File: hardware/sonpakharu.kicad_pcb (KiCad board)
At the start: 2 copper layers, 51.3 x 71.1 mm, 70 parts, among them IC1 ESP32-S3-WROOM-1U-N4, J1 ADC4, J10 EXT2, J11 EXT3, J12 BATT, J13 EXT7, J14 PWR, J15 EXT8, J16 485, J17 FTDI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

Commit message: Fix: final fixes
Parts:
- moved sp 1.67 mm to (126.9, 64.9)
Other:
- board text added: "Sonpakhru"
- board text added: "sonpakhru.com"
- board text removed: "Sonpakharu"

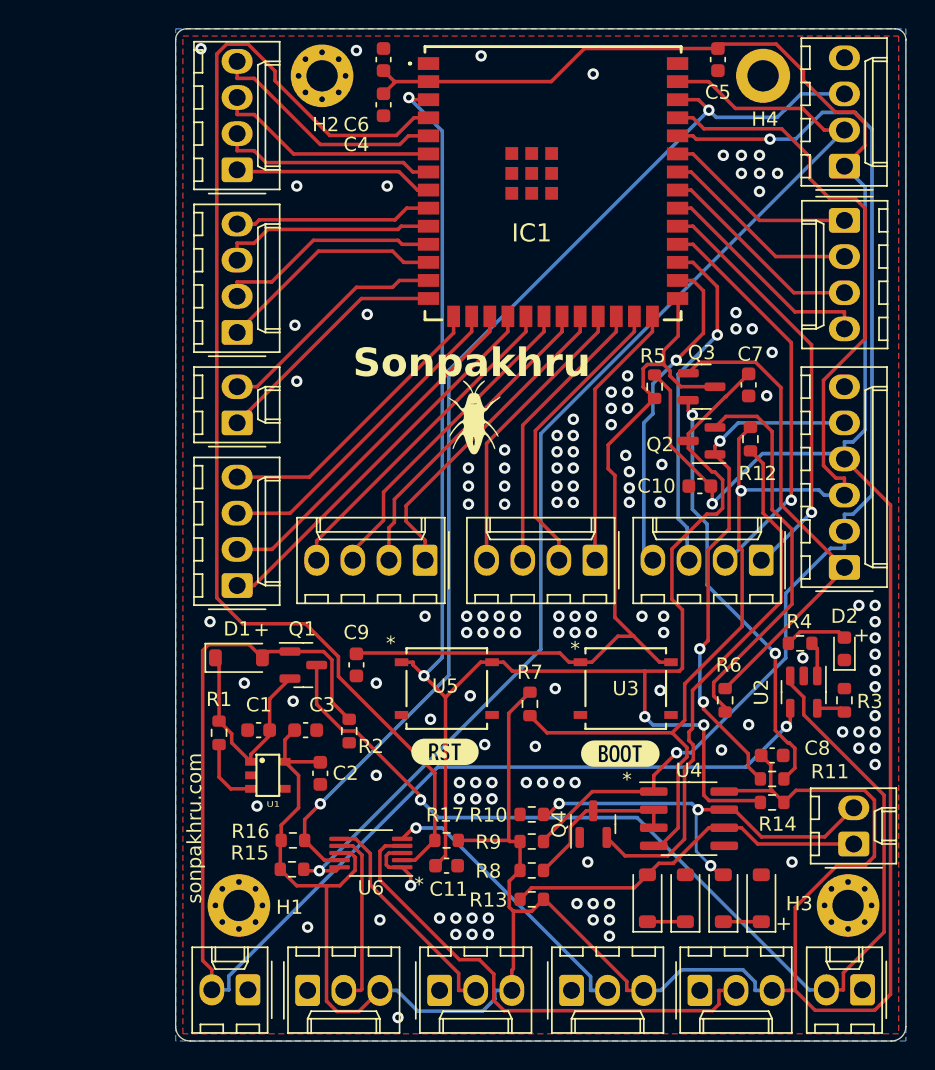
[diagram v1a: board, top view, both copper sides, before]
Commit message: rectified sch
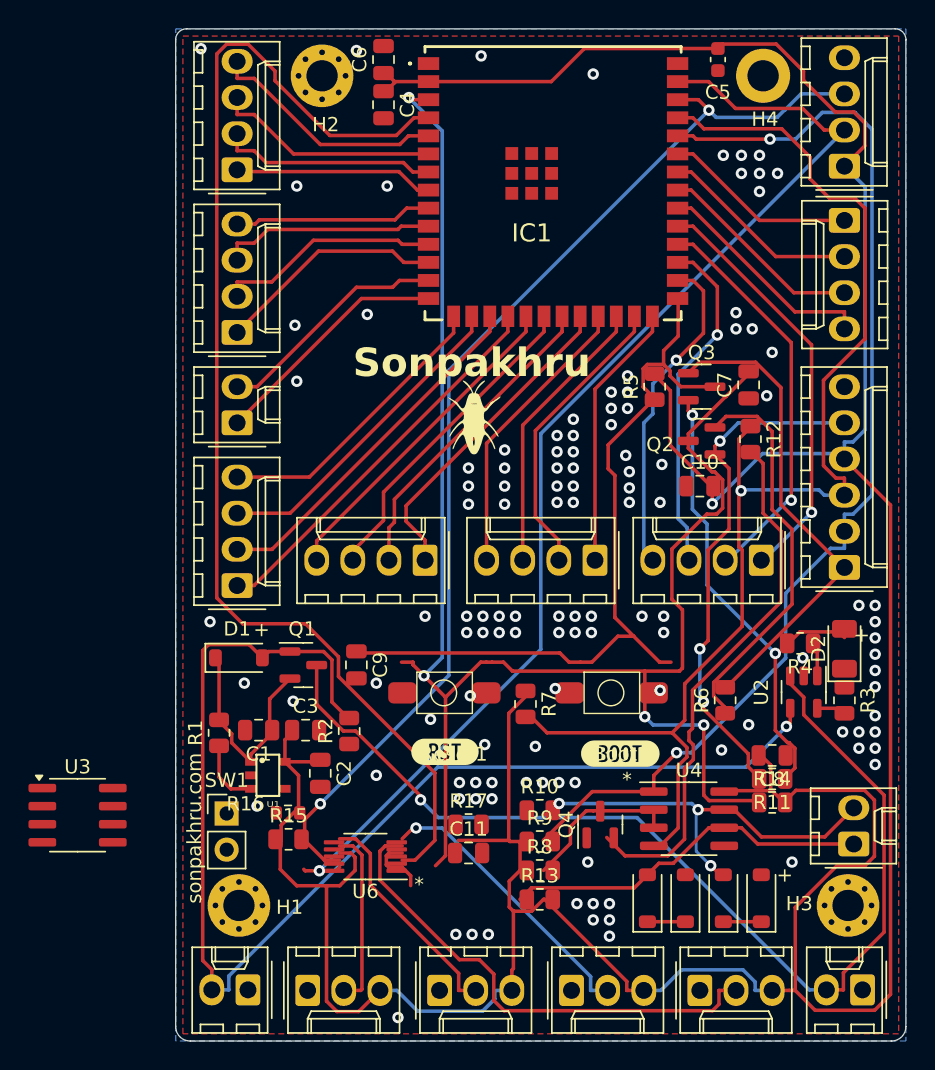
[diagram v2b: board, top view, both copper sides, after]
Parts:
- removed U5: Reset, PTS526 SK15 SMTR2 LFS:SMT_FS
- added Boot1: Boot, tactile_5.4:tactile_5.4, F.Cu at (136.5, 84.2)
- added Reset1: Reset, tactile_5.4:tactile_5.4, F.Cu at (124.8, 84.2)
- added SW1: ON/OFF, Connector_PinHeader_2.54mm:PinHeader_1x02_P2.54mm_Vertical, F.Cu at (109.5, 92.7)
- C1, C10, C11, C2, C3, C4, C6, C7, C8, C9: footprint Capacitor_SMD:C_0603_1608Metric -> Capacitor_SMD:C_0805_2012Metric
- D2: footprint LED_SMD:LED_0603_1608Metric -> LED_SMD:LED_1206_3216Metric
- J17: value FTDI -> ESP PRG
- R1, R10, R11, R12, R13, R14, R15, R17, R2, R3, R4, R5, R6, R7, R8, R9: footprint Resistor_SMD:R_0603_1608Metric -> Resistor_SMD:R_0805_2012Metric
- U3: value Boot -> MCP3426Axx-xSN; footprint PTS526 SK15 SMTR2 LFS:SMT_FS -> Package_SO:SOIC-8_3.9x4.9mm_P1.27mm
- moved U3 39.5 mm to (99.0, 92.8)
- moved R15 2.12 mm to (113.9, 94.5)
- moved R16 1.96 mm to (113.8, 92.7)
- moved R17 1.91 mm to (126.5, 93.5)
- moved C11 1.79 mm to (126.5, 95.5)
- moved R10 0.63 mm to (131.5, 92.5)
- moved R13 0.56 mm to (131.5, 98.8)
- moved R8 0.56 mm to (131.5, 96.7)
- moved R9 0.56 mm to (131.5, 94.7)
- moved Q4 0.50 mm to (135.8, 93.5)
- moved U6 0.46 mm to (119.2, 95.8)
- moved R7 0.31 mm to (130.5, 85.0)
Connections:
- net /GP1 renamed /IO5
- net /GP10 renamed /IO20
- net /GP11 renamed /IO3
- net /GP12 renamed /IO46
- net /GP13 renamed /IO9
- net /GP14 renamed /IO10
- net /GP15 renamed /IO11
- net /GP16 renamed /IO12
- net /GP17 renamed /IO13
- net /GP18 renamed /IO14
- net /GP19 renamed /IO21
- net /GP2 renamed /IO6
- net /GP20 renamed /IO47
- net /GP21 renamed /IO48
- net /GP22 renamed /IO45
- net /GP23 renamed /IO35
- net /GP24 renamed /IO36
- net /GP25 renamed /IO37
- net /GP26 renamed /IO38
- net /GP27 renamed /IO39
- net /GP28 renamed /IO40
- net /GP29 renamed /IO41
- net /GP3 renamed /IO7
- net /GP30 renamed /IO42
- net /GP4 renamed /IO15
- net /GP5 renamed /IO16
- net /GP6 renamed /IO17
- net /GP7 renamed /IO18
- net /GP8 renamed /IO8
- net /GP9 renamed /IO19
- J17 pad 1: /DTR -> +3V3
- J17 pad 4: +3V3 -> GND
- J17 pad 5: /RTS -> /EN
- J17 pad 6: GND -> /IO0
- R15 pad 2: /SCL -> Net-(U3-SCL)
- R16 pad 2: /SDA -> Net-(U3-SDA)
- U1 pad 5: +3V3 -> Net-(SW1-A)
- U3 pad 1: /IO0 -> /A0
- U3 pad 2: /IO0 -> GND
- U3 pad 3: GND -> +3V3
- U3 pad 4: GND -> Net-(U3-SDA)
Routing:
- net GND: vias 127 -> 120

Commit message: deleted unused footprints
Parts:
- removed R17: 10K, Resistor_SMD:R_0805_2012Metric
- removed U6: ADS1115IDGSR, Package_SO:VSSOP-10_3x3mm_P0.5mm
- moved U3 21.3 mm to (120.0, 96.5)
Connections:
- U3 pad 1: /A0 -> unconnected-(U3-CH1+-Pad1)
- U3 pad 7: /A1 -> unconnected-(U3-CH2+-Pad7)

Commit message: removed auto prg ckt, done routing, touch up pending
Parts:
- removed C7: 4.7uF, Capacitor_SMD:C_0805_2012Metric
- removed C9: 1uF, Capacitor_SMD:C_0805_2012Metric
- removed J1: ADC4, Connector_Molex:Molex_KK-254_AE-6410-03A_1x03_P2.54mm_Vertical
- removed J2: ADC3, Connector_Molex:Molex_KK-254_AE-6410-03A_1x03_P2.54mm_Vertical
- removed Q2: S8050, Package_TO_SOT_SMD:SOT-23
- removed Q3: SS8050-G, Package_TO_SOT_SMD:SOT-23
- removed R11, R6: 12K, Resistor_SMD:R_0805_2012Metric
- C5: footprint Capacitor_SMD:C_0603_1608Metric -> Capacitor_SMD:C_0805_2012Metric
- R16: footprint Resistor_SMD:R_0603_1608Metric -> Resistor_SMD:R_0805_2012Metric
- moved R16 2.13 mm to (113.8, 94.8)
- moved R15 1.79 mm to (113.8, 92.8)
- moved C4 0.68 mm to (120.5, 43.6)
- moved R5 0.49 mm to (139.6, 63.2), turned to -90 degrees
- moved R1 0.47 mm to (108.5, 87.0)
- moved C1 0.25 mm to (111.5, 86.9)
- moved R2 0.14 mm to (118.2, 86.9)
- turned R13 to 180 degrees
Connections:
- U3 pad 1: unconnected-(U3-CH1+-Pad1) -> /A0
- U3 pad 7: unconnected-(U3-CH2+-Pad7) -> /A1
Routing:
- net /IO4: track 85.8 -> 0.00 mm
- net /SCL: track 83.1 -> 13.1 mm, vias 1 -> 0
- net /SDA: track 79.0 -> 12.9 mm, vias 2 -> 1
- net /RTS: track 36.2 -> 0.00 mm, vias 3 -> 0
- net /DTR: track 34.0 -> 0.00 mm
- net Net-(Q3-B): track 30.1 -> 0.00 mm, vias 2 -> 0
- net Net-(Q2-B): track 27.7 -> 0.00 mm
- net +3V3: track 260.6 -> 278.7 mm
- net /A2: track 16.0 -> 0.00 mm
- net /A3: track 12.6 -> 0.00 mm
- net Net-(U3-SCL): track 0.00 -> 11.5 mm
- net /IO0: track 56.2 -> 49.7 mm, vias 0 -> 4
- net Net-(SW1-A): track 0.00 -> 6.47 mm
- net Net-(U3-SDA): track 0.00 -> 5.69 mm
- net GND: track 4.55 -> 0.25 mm, vias 120 -> 126
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
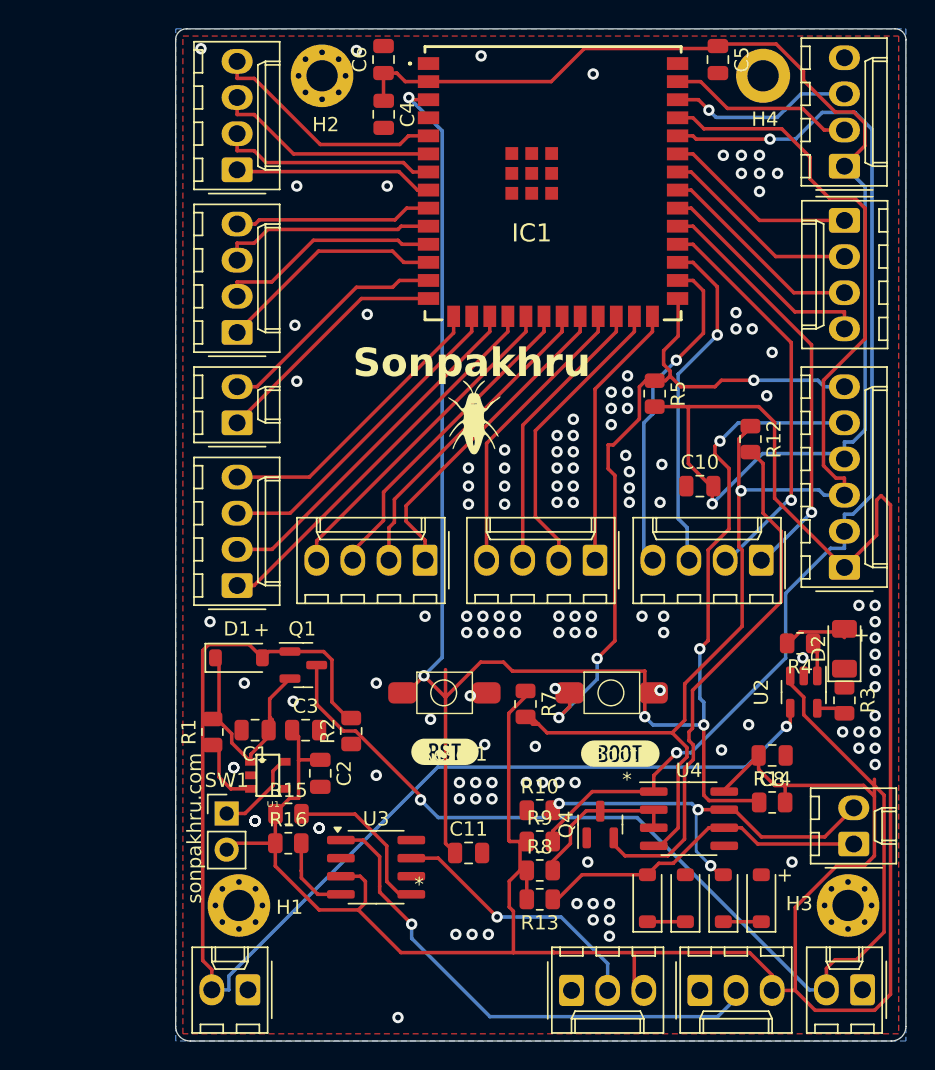
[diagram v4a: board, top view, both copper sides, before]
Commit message: corrected signal tracks
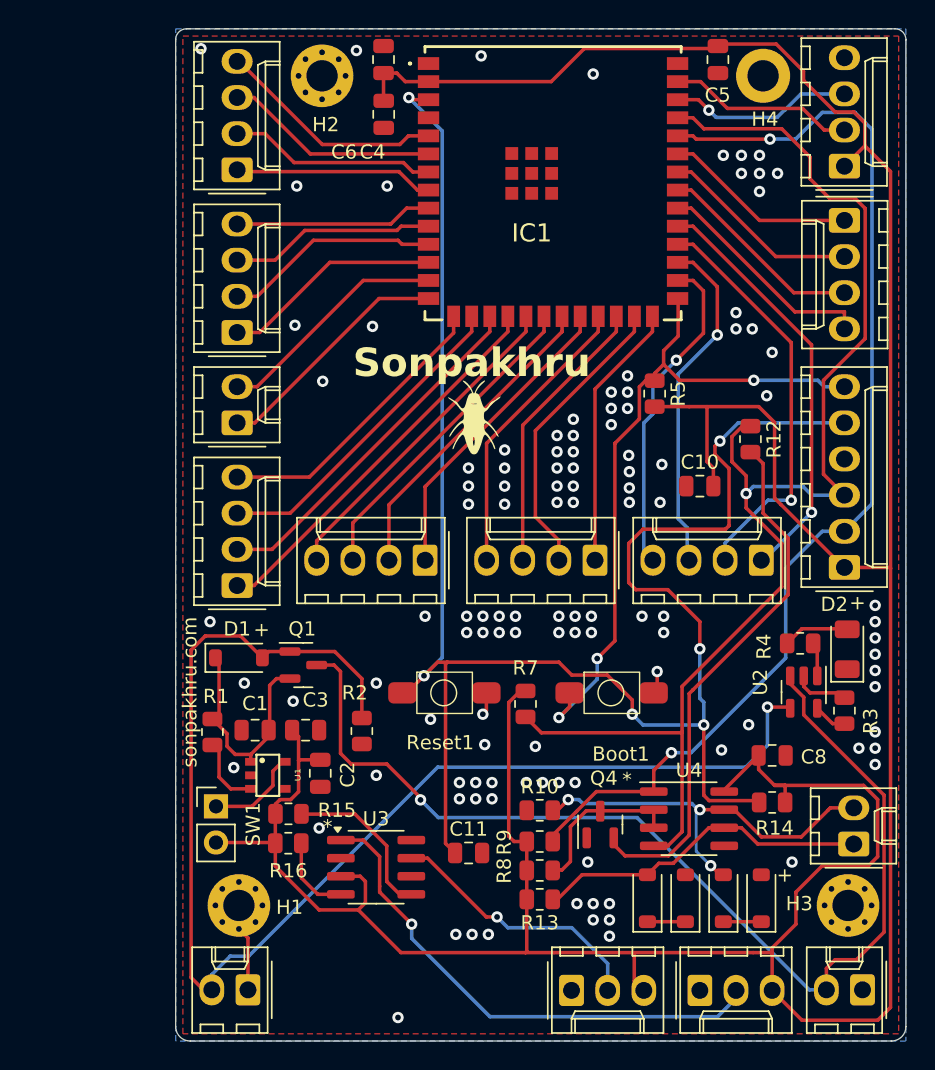
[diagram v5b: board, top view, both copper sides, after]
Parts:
- removed kibuzzard-65BFB976: G***, kibuzzard-65BFB976
- removed kibuzzard-65BFB983: G***, kibuzzard-65BFB983
- moved SW1 0.90 mm to (108.8, 92.2)
- moved R2 0.75 mm to (119.0, 86.9)
- moved R3 0.73 mm to (152.9, 85.5)
- moved D2 0.20 mm to (153.1, 81.2)
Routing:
- net +3V3: track 278.7 -> 263.9 mm, vias 1 -> 0
- net GND: track 0.25 -> 12.3 mm, vias 126 -> 115
- net /EN: track 123.7 -> 130.6 mm
- net VBUS: track 88.9 -> 92.7 mm
- net +BATT: track 74.4 -> 76.3 mm
- net /TX: track 92.4 -> 94.2 mm
- net /RX: track 78.8 -> 77.6 mm
- net /IO14: track 22.8 -> 21.7 mm
- net /IO0: track 49.7 -> 48.7 mm, vias 4 -> 3
- net /IO37: track 28.3 -> 29.2 mm
- net /IO7: track 15.3 -> 14.6 mm
- net /IO17: track 15.1 -> 14.4 mm
- net /IO6: track 15.8 -> 15.1 mm
- net /IO5: track 16.8 -> 16.1 mm
- net /IO8: track 16.1 -> 15.5 mm
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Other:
- board text removed: "A2"
- board text removed: "A3"

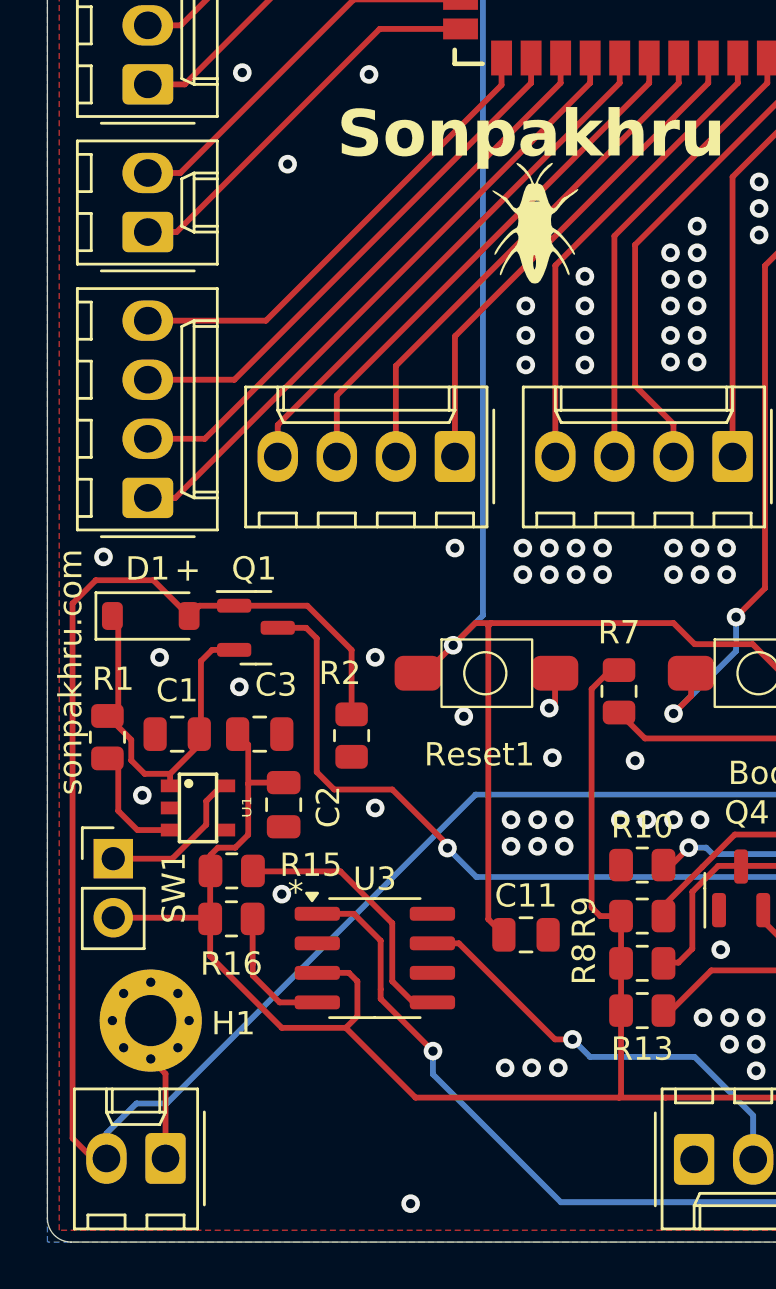
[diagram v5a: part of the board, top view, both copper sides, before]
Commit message: added IO4 pin to connector
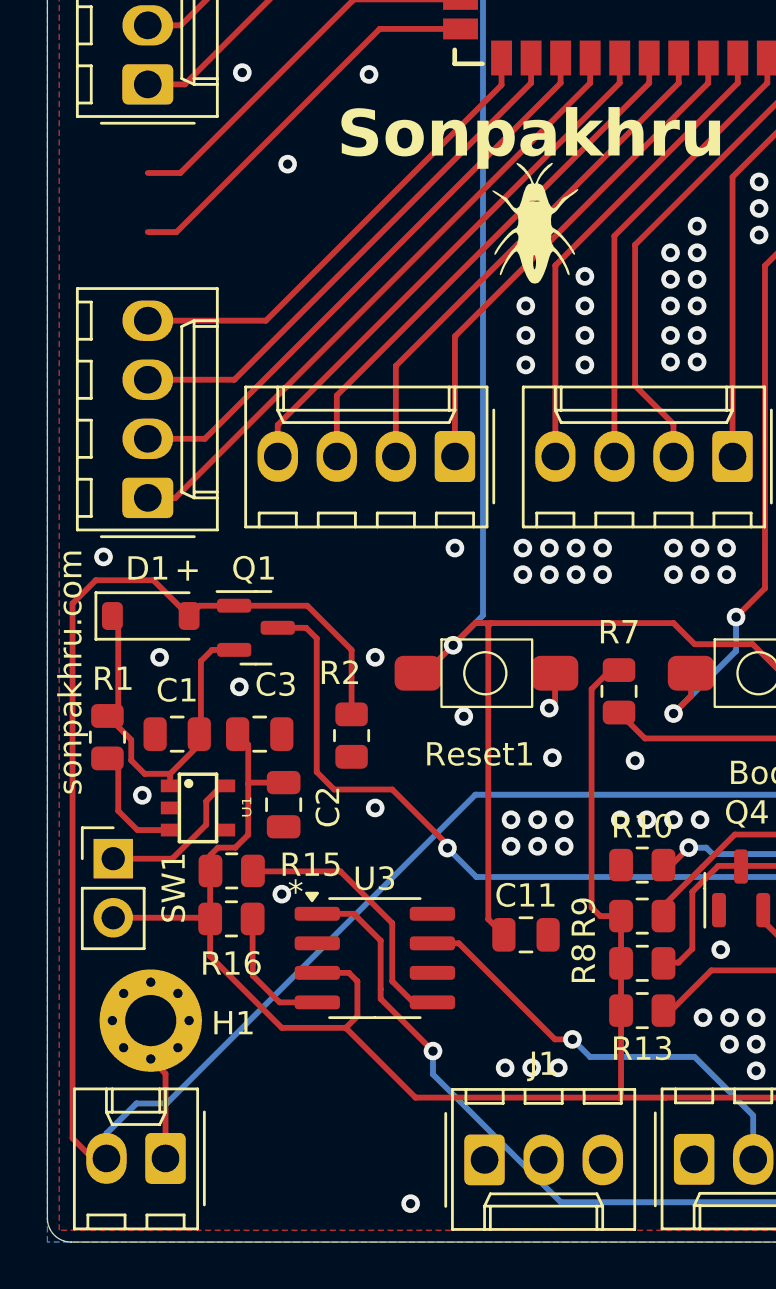
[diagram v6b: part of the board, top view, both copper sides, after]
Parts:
- removed J11: EXT3, Connector_Molex:Molex_KK-254_AE-6410-02A_1x02_P2.54mm_Vertical
- added J1: ADC1, Connector_Molex:Molex_KK-254_AE-6410-03A_1x03_P2.54mm_Vertical, F.Cu at (124.7, 105.2)
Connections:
- R15 pad 2: Net-(U3-SCL) -> /SCL
- R16 pad 2: Net-(U3-SDA) -> /SDA
- U3 pad 4: Net-(U3-SDA) -> /SDA
- U3 pad 5: Net-(U3-SCL) -> /SCL
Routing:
- net Net-(U3-SCL): track 11.5 -> 0.00 mm
- net /SCL: track 13.1 -> 24.7 mm
- net /SDA: track 12.9 -> 18.6 mm
- net Net-(U3-SDA): track 5.69 -> 0.00 mm
